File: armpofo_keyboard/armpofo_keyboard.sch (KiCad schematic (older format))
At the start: 94 parts, among them J1 Conn_01x16, M1 2,5mm, M10 2,5mm, M11 2,5mm, M12 2,5mm, M13 2,5mm, M14 2,5mm, M15 2,5mm, M16 2,5mm, M17 2,5mm, M18 2,5mm, M2 2,5mm, M3 2,5mm, M4 2,5mm, M5 2,5mm, M6 2,5mm, M7 2,5mm, M8 2,5mm, M9 2,5mm, SW1 Backspace, SW10 4, SW11 3, SW12 2, SW13 1, SW14 ESC, SW15 ], SW16 [, SW17 P, SW18 O, SW19 I, SW2 =+, SW20 U, SW21 Y, SW22 T, SW23 R, SW24 E, SW25 W, SW26 Q, SW27 TAB, SW28 ENTER, SW29 CAPS, SW3 -_, SW30 ' \", SW31 ;:, SW32 L, SW33 K, SW34 J, SW35 H, SW36 G, SW37 F, SW38 D, SW39 S, SW4 0, SW40 A, SW41 RSH, SW42 INS DEL, SW43 /?, SW44 .>, SW45 ,<, SW46 M, SW47 N, SW48 B, SW49 V, SW5 9, SW50 C, SW51 X, SW52 Z, SW53 \\|, SW54 LSH, SW55 RIGHT, SW56 DOWN, SW57 UP, SW58 LEFT, SW59 SPACE, SW6 8, SW60 SPACE, SW61 ALT, SW62 CTRL, SW63 ATARI, SW64 FN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

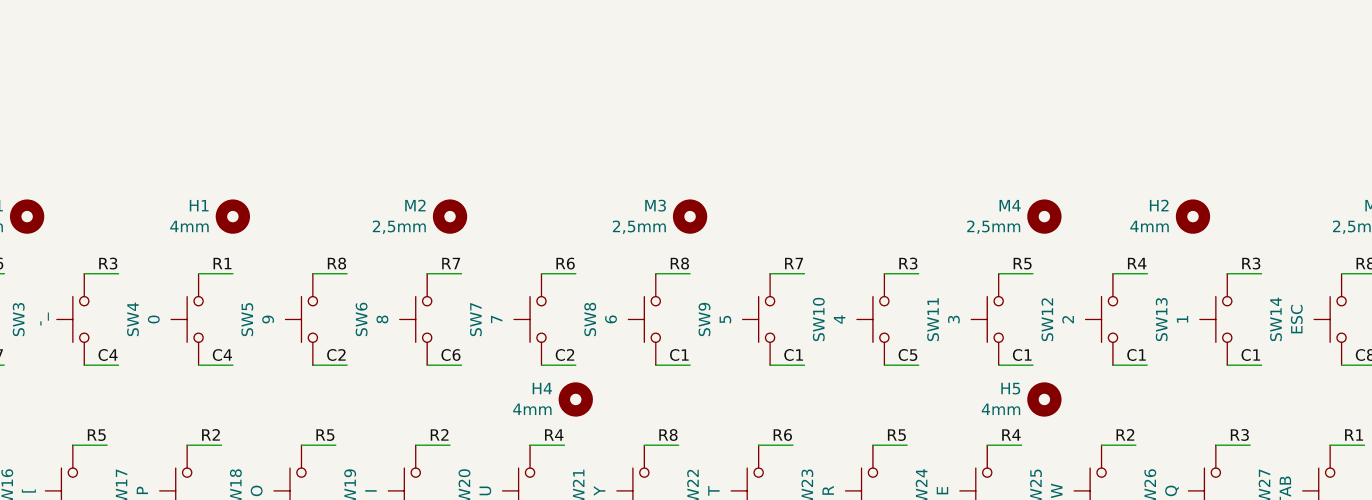
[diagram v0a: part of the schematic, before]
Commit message: edge cut correction
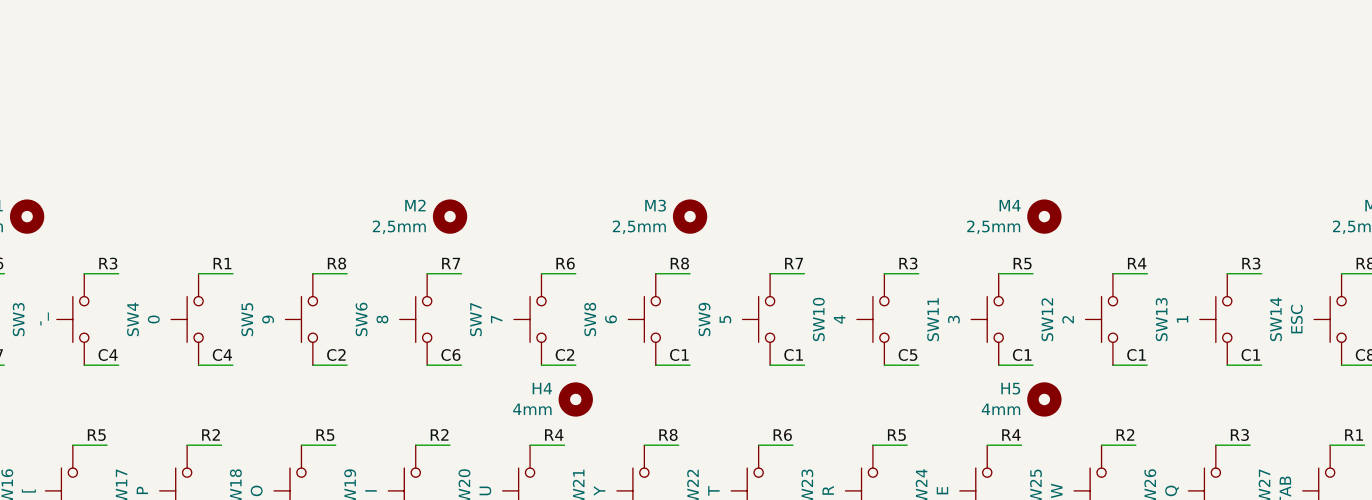
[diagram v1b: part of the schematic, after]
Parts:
- removed H1, H2: 4mm, MountingHole:MountingHole_4mm, symbol Mechanical:MountingHole
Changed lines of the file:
@@
 R7
-$Comp
-L Mechanical:MountingHole H2
-U 1 1 5F9F6D1C
-P 9000 1600
-F 0 "H2" H 9100 1646 50  0000 L CNN
-F 1 "4mm" H 9100 1555 50  0000 L CNN
-F 2 "MountingHole:MountingHole_4mm" H 9000 1600 50  0001 C CNN
-F 3 "~" H 9000 1600 50  0001 C CNN
-	1    9000 1600
-	-1   0    0    -1
-$EndComp
-$Comp
-L Mechanical:MountingHole H1
-U 1 1 5FA27CB1
-P 4800 1600
-F 0 "H1" H 4900 1646 50  0000 L CNN
-F 1 "4mm" H 4900 1555 50  0000 L CNN
-F 2 "MountingHole:MountingHole_4mm" H 4800 1600 50  0001 C CNN
-F 3 "~" H 4800 1600 50  0001 C CNN
-	1    4800 1600
-	-1   0    0    -1
-$EndComp
 $Comp
 L Mechanical:MountingHole H3

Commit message: routing finished
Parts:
- M1, M10, M11, M12, M13, M14, M15, M16, M17, M18, M2, M3, M4, M5, M6, M7, M8, M9: symbol Mechanical:MountingHole -> Mechanical:MountingHole_Pad
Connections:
- new net GND: M1.1, M10.1, M11.1, M12.1, M13.1, M14.1, M15.1, M16.1, M17.1, M18.1, M2.1, M3.1, M4.1, M5.1, M6.1, M7.1, M8.1, M9.1

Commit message: - CPU board finalisch edge cuts - Keyboard mounting modified to 2.2 mm holes
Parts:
- M1, M10, M11, M12, M13, M14, M15, M16, M17, M18, M2, M3, M4, M5, M6, M7, M8, M9: value 2,5mm -> 2,1mm; footprint MountingHole:MountingHole_2.5mm_Pad -> MountingHole:MountingHole_2.2mm_M2_DIN965_Pad
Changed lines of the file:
@@
 P 2800 1400
 F 0 "M6" H 2900 1446 50  0000 L CNN
-F 1 "2,5mm" H 2900 1355 50  0000 L CNN
-F 2 "MountingHole:MountingHole_2.5mm_Pad" H 2800 1400 50  0001 C CNN
+F 1 "2,1mm" H 2900 1355 50  0000 L CNN
+F 2 "MountingHole:MountingHole_2.2mm_M2_DIN965_Pad" H 2800 1400 50  0001 C CNN
 F 3 "~" H 2800 1400 50  0001 C CNN
 	1    2800 1400
@@
 P 2800 3600
 F 0 "M10" H 2900 3646 50  0000 L CNN
-F 1 "2,5mm" H 2900 3555 50  0000 L CNN
-F 2 "MountingHole:MountingHole_2.5mm_Pad" H 2800 3600 50  0001 C CNN
+F 1 "2,1mm" H 2900 3555 50  0000 L CNN
+F 2 "MountingHole:MountingHole_2.2mm_M2_DIN965_Pad" H 2800 3600 50  0001 C CNN
 F 3 "~" H 2800 3600 50  0001 C CNN
 	1    2800 3600
@@
 P 2900 5450
 F 0 "M13" H 3000 5496 50  0000 L CNN
-F 1 "2,5mm" H 3000 5405 50  0000 L CNN
-F 2 "MountingHole:MountingHole_2.5mm_Pad" H 2900 5450 50  0001 C CNN
+F 1 "2,1mm" H 3000 5405 50  0000 L CNN
+F 2 "MountingHole:MountingHole_2.2mm_M2_DIN965_Pad" H 2900 5450 50  0001 C CNN
 F 3 "~" H 2900 5450 50  0001 C CNN
 	1    2900 5450
@@
 P 4450 5500
 F 0 "M16" H 4550 5546 50  0000 L CNN
-F 1 "2,5mm" H 4550 5455 50  0000 L CNN
-F 2 "MountingHole:MountingHole_2.5mm_Pad" H 4450 5500 50  0001 C CNN
+F 1 "2,1mm" H 4550 5455 50  0000 L CNN
+F 2 "MountingHole:MountingHole_2.2mm_M2_DIN965_Pad" H 4450 5500 50  0001 C CNN
 F 3 "~" H 4450 5500 50  0001 C CNN
 	1    4450 5500
@@
 P 5350 5500
 F 0 "M17" H 5450 5546 50  0000 L CNN
-F 1 "2,5mm" H 5450 5455 50  0000 L CNN
-F 2 "MountingHole:MountingHole_2.5mm_Pad" H 5350 5500 50  0001 C CNN
+F 1 "2,1mm" H 5450 5455 50  0000 L CNN
+F 2 "MountingHole:MountingHole_2.2mm_M2_DIN965_Pad" H 5350 5500 50  0001 C CNN
 F 3 "~" H 5350 5500 50  0001 C CNN
 	1    5350 5500
@@
 P 7150 5500
 F 0 "M18" H 7250 5546 50  0000 L CNN
-F 1 "2,5mm" H 7250 5455 50  0000 L CNN
-F 2 "MountingHole:MountingHole_2.5mm_Pad" H 7150 5500 50  0001 C CNN
+F 1 "2,1mm" H 7250 5455 50  0000 L CNN
+F 2 "MountingHole:MountingHole_2.2mm_M2_DIN965_Pad" H 7150 5500 50  0001 C CNN
 F 3 "~" H 7150 5500 50  0001 C CNN
 	1    7150 5500
@@
 P 8400 5450
 F 0 "M14" H 8500 5496 50  0000 L CNN
-F 1 "2,5mm" H 8500 5405 50  0000 L CNN
-F 2 "MountingHole:MountingHole_2.5mm_Pad" H 8400 5450 50  0001 C CNN
+F 1 "2,1mm" H 8500 5405 50  0000 L CNN
+F 2 "MountingHole:MountingHole_2.2mm_M2_DIN965_Pad" H 8400 5450 50  0001 C CNN
 F 3 "~" H 8400 5450 50  0001 C CNN
 	1    8400 5450
@@
 P 10000 5450
 F 0 "M15" H 10100 5496 50  0000 L CNN
-F 1 "2,5mm" H 10100 5405 50  0000 L CNN
-F 2 "MountingHole:MountingHole_2.5mm_Pad" H 10000 5450 50  0001 C CNN
+F 1 "2,1mm" H 10100 5405 50  0000 L CNN
+F 2 "MountingHole:MountingHole_2.2mm_M2_DIN965_Pad" H 10000 5450 50  0001 C CNN
 F 3 "~" H 10000 5450 50  0001 C CNN
 	1    10000 5450
@@
 P 10000 3850
 F 0 "M12" H 10100 3896 50  0000 L CNN
-F 1 "2,5mm" H 10100 3805 50  0000 L CNN
-F 2 "MountingHole:MountingHole_2.5mm_Pad" H 10000 3850 50  0001 C CNN
+F 1 "2,1mm" H 10100 3805 50  0000 L CNN
+F 2 "MountingHole:MountingHole_2.2mm_M2_DIN965_Pad" H 10000 3850 50  0001 C CNN
 F 3 "~" H 10000 3850 50  0001 C CNN
 	1    10000 3850
@@
 P 9950 1350
 F 0 "M5" H 10050 1396 50  0000 L CNN
-F 1 "2,5mm" H 10050 1305 50  0000 L CNN
-F 2 "MountingHole:MountingHole_2.5mm_Pad" H 9950 1350 50  0001 C CNN
+F 1 "2,1mm" H 10050 1305 50  0000 L CNN
+F 2 "MountingHole:MountingHole_2.2mm_M2_DIN965_Pad" H 9950 1350 50  0001 C CNN
 F 3 "~" H 9950 1350 50  0001 C CNN
 	1    9950 1350
@@
 P 8350 1350
 F 0 "M4" H 8450 1396 50  0000 L CNN
-F 1 "2,5mm" H 8450 1305 50  0000 L CNN
-F 2 "MountingHole:MountingHole_2.5mm_Pad" H 8350 1350 50  0001 C CNN
+F 1 "2,1mm" H 8450 1305 50  0000 L CNN
+F 2 "MountingHole:MountingHole_2.2mm_M2_DIN965_Pad" H 8350 1350 50  0001 C CNN
 F 3 "~" H 8350 1350 50  0001 C CNN
 	1    8350 1350
@@
 P 6800 1350
 F 0 "M3" H 6900 1396 50  0000 L CNN
-F 1 "2,5mm" H 6900 1305 50  0000 L CNN
-F 2 "MountingHole:MountingHole_2.5mm_Pad" H 6800 1350 50  0001 C CNN
+F 1 "2,1mm" H 6900 1305 50  0000 L CNN
+F 2 "MountingHole:MountingHole_2.2mm_M2_DIN965_Pad" H 6800 1350 50  0001 C CNN
 F 3 "~" H 6800 1350 50  0001 C CNN
 	1    6800 1350
@@
 P 5750 1350
 F 0 "M2" H 5850 1396 50  0000 L CNN
-F 1 "2,5mm" H 5850 1305 50  0000 L CNN
-F 2 "MountingHole:MountingHole_2.5mm_Pad" H 5750 1350 50  0001 C CNN
+F 1 "2,1mm" H 5850 1305 50  0000 L CNN
+F 2 "MountingHole:MountingHole_2.2mm_M2_DIN965_Pad" H 5750 1350 50  0001 C CNN
 F 3 "~" H 5750 1350 50  0001 C CNN
 	1    5750 1350
@@
 P 3900 1350
 F 0 "M1" H 4000 1396 50  0000 L CNN
-F 1 "2,5mm" H 4000 1305 50  0000 L CNN
-F 2 "MountingHole:MountingHole_2.5mm_Pad" H 3900 1350 50  0001 C CNN
+F 1 "2,1mm" H 4000 1305 50  0000 L CNN
+F 2 "MountingHole:MountingHole_2.2mm_M2_DIN965_Pad" H 3900 1350 50  0001 C CNN
 F 3 "~" H 3900 1350 50  0001 C CNN
 	1    3900 1350
@@
 P 3750 3150
 F 0 "M7" H 3850 3196 50  0000 L CNN
-F 1 "2,5mm" H 3850 3105 50  0000 L CNN
-F 2 "MountingHole:MountingHole_2.5mm_Pad" H 3750 3150 50  0001 C CNN
+F 1 "2,1mm" H 3850 3105 50  0000 L CNN
+F 2 "MountingHole:MountingHole_2.2mm_M2_DIN965_Pad" H 3750 3150 50  0001 C CNN
 F 3 "~" H 3750 3150 50  0001 C CNN
 	1    3750 3150
@@
 P 5250 3150
 F 0 "M8" H 5350 3196 50  0000 L CNN
-F 1 "2,5mm" H 5350 3105 50  0000 L CNN
-F 2 "MountingHole:MountingHole_2.5mm_Pad" H 5250 3150 50  0001 C CNN
+F 1 "2,1mm" H 5350 3105 50  0000 L CNN
+F 2 "MountingHole:MountingHole_2.2mm_M2_DIN965_Pad" H 5250 3150 50  0001 C CNN
 F 3 "~" H 5250 3150 50  0001 C CNN
 	1    5250 3150
@@
 P 8300 3150
 F 0 "M9" H 8400 3196 50  0000 L CNN
-F 1 "2,5mm" H 8400 3105 50  0000 L CNN
-F 2 "MountingHole:MountingHole_2.5mm_Pad" H 8300 3150 50  0001 C CNN
+F 1 "2,1mm" H 8400 3105 50  0000 L CNN
+F 2 "MountingHole:MountingHole_2.2mm_M2_DIN965_Pad" H 8300 3150 50  0001 C CNN
 F 3 "~" H 8300 3150 50  0001 C CNN
 	1    8300 3150
@@
 P 7050 3850
 F 0 "M11" H 7150 3896 50  0000 L CNN
-F 1 "2,5mm" H 7150 3805 50  0000 L CNN
-F 2 "MountingHole:MountingHole_2.5mm_Pad" H 7050 3850 50  0001 C CNN
+F 1 "2,1mm" H 7150 3805 50  0000 L CNN
+F 2 "MountingHole:MountingHole_2.2mm_M2_DIN965_Pad" H 7050 3850 50  0001 C CNN
 F 3 "~" H 7050 3850 50  0001 C CNN
 	1    7050 3850
